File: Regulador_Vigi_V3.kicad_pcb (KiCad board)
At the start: 2 copper layers, 50 x 35 mm, 15 parts, among them J1 IN, J2 Out, U1 LM5163

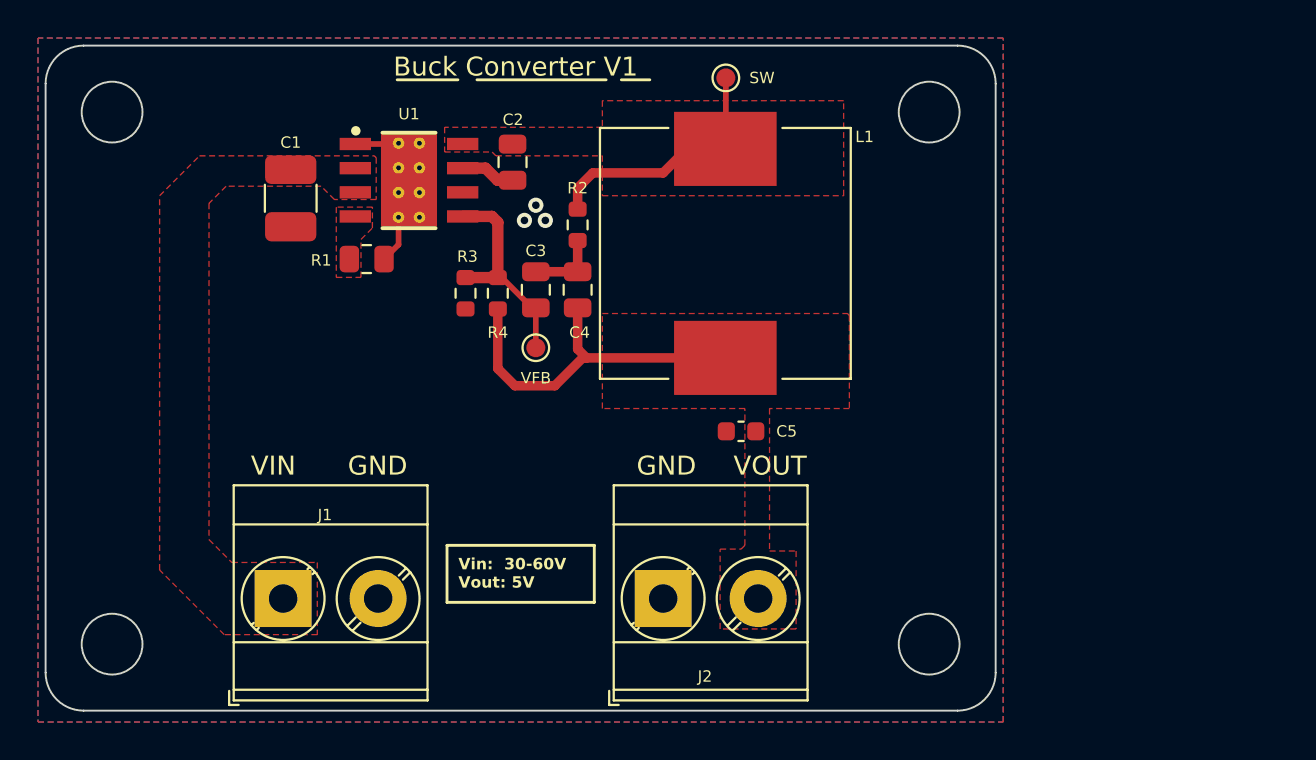
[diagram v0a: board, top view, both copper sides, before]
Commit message: SCH: Se cambiaron las resistencias del feedback, se limpiaron los comentarios. PCB: Se terminó de rutear. GITIGNORE: se agregó una línea
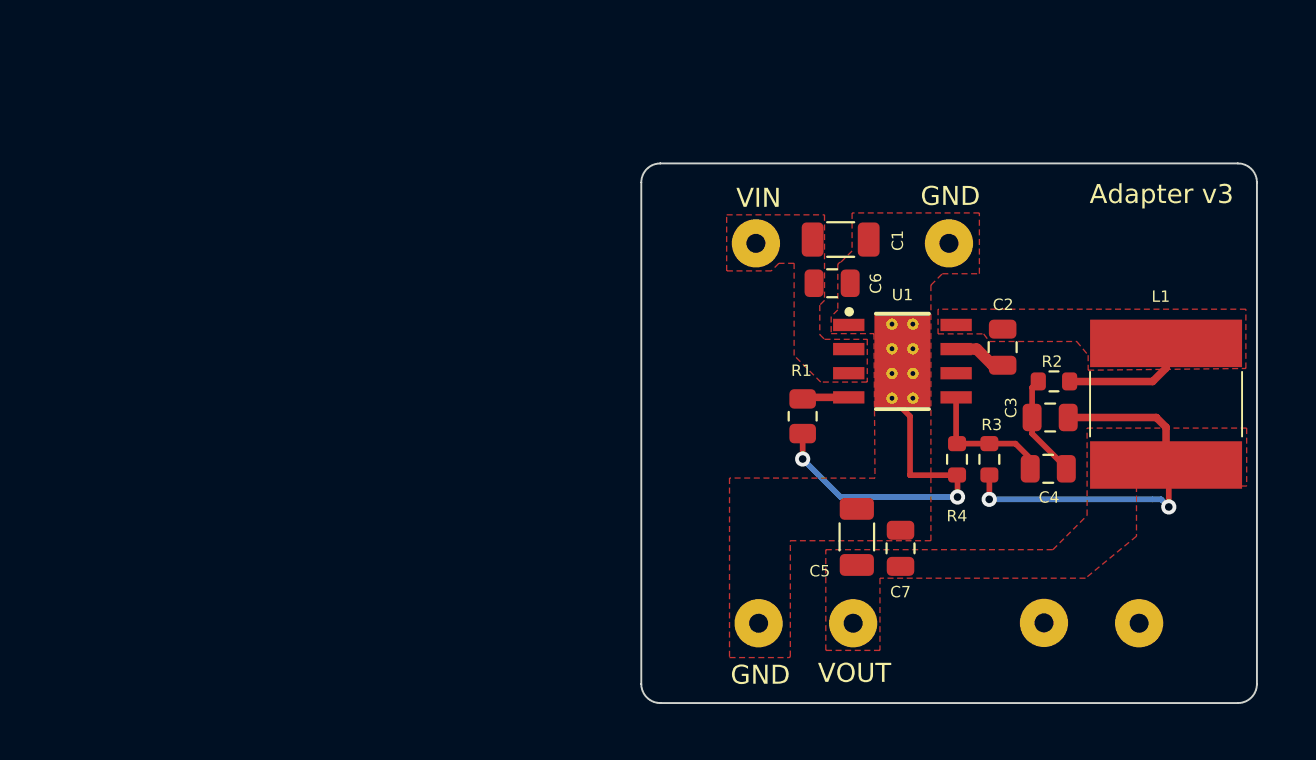
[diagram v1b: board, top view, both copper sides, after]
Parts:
- removed J1: IN, 1-Terminal-Block:AK700-DG129-1x02_P5.00mm
- removed J2: Out, 1-Terminal-Block:AK700-DG129-1x02_P5.00mm
- removed TP1: VFB, TestPoint:TestPoint_Pad_D1.0mm
- removed TP2: SW, TestPoint:TestPoint_Pad_D1.0mm
- added C6: 100nF 50V, 1-Capacitor:C_0805_2012Metric, F.Cu at (174.5, 120.5)
- added C7: 100nF 50V, 1-Capacitor:C_0805_2012Metric, F.Cu at (178.1, 134.5)
- added PAD1: PAD_2.54_1.0, 1-Pad:PAD_2.54_1.0, F.Cu at (172.7, 118.3)
- added PAD2: PAD_2.54_1.0, 1-Pad:PAD_2.54_1.0, F.Cu at (170.6, 138.4)
- added PAD3: PAD_2.54_1.0, 1-Pad:PAD_2.54_1.0, F.Cu at (175.6, 138.4)
- added PAD4: PAD_2.54_1.0, 1-Pad:PAD_2.54_1.0, F.Cu at (180.6, 118.4)
- added PAD5: PAD_2.54_1.0, 1-Pad:PAD_2.54_1.0, F.Cu at (185.6, 138.4)
- added PAD6: PAD_2.54_1.0, 1-Pad:PAD_2.54_1.0, F.Cu at (190.7, 138.4)
- C1: value 2.2uF 100V -> 4.7uF 50V; footprint 1-Capacitor:C_1210_3225Metric_Mod -> 1-Capacitor:C_1206_3216Metric
- C3: value 2.2nF 50V -> 1.2nF 50V
- C4: value 56pF 50V -> 47pF 50V
- C5: value 2.2uF 16V -> 4.7uF 50V; footprint 1-Capacitor:C_0603_1608Metric -> 1-Capacitor:C_1206_3216Metric
- L1: value SMDRI127-331MT -> 100uH 1A; footprint 1-Inductor:DR127 -> 1-Inductor:L_8x8mm
- R1: value 43k -> 150k
- R2: value 316k -> 130k
- R3: value 316k -> 210k
- R4: value 100k -> 15k
- moved C1 29.0 mm to (174.9, 118.2), turned to 0 degrees
- moved C4 28.6 mm to (185.9, 130.3), turned to 180 degrees
- moved U1 27.7 mm to (178.2, 124.6)
- moved C2 27.6 mm to (183.5, 123.9)
- moved R4 27.3 mm to (181.1, 129.8)
- moved R3 27.3 mm to (182.8, 129.8)
- moved R2 26.4 mm to (186.2, 125.7), turned to 180 degrees
- moved C3 25.8 mm to (186.0, 127.6), turned to 180 degrees
- moved L1 24.5 mm to (192.1, 126.9)
- moved R1 24.4 mm to (172.9, 127.5), turned to -90 degrees
- moved C5 8.25 mm to (175.8, 133.9), turned to 90 degrees
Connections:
- net +5V renamed VOUT
- U1 pad 10: GND -> (no net)
- U1 pad 11: GND -> (no net)
- U1 pad 12: GND -> (no net)
- U1 pad 13: GND -> (no net)
- U1 pad 14: GND -> (no net)
- U1 pad 15: GND -> (no net)
- U1 pad 16: GND -> (no net)
- U1 pad 17: GND -> (no net)
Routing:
- net GND: track 4.81 -> 18.4 mm, vias 3 -> 2
- net Net-(U1-SW): track 15.3 -> 6.67 mm
- net Net-(U1-FB): track 11.3 -> 7.18 mm
- net Net-(U1-RON): track 0.00 -> 2.46 mm
- net VOUT: track 18.9 -> 21.0 mm, vias 0 -> 2
- net Net-(C3-Pad2): track 3.84 -> 5.48 mm
- removed copper zone on B.Cu, net GND
- removed copper zone on F.Cu, net Net-(U1-RON)
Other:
- board size 50 x 35 mm -> 32.4 x 28.4 mm
- board text added: "Adapter v3"
- board text removed: "Buck Converter V1"
- board text removed: "Vin: 30-60V Vout: 5V"

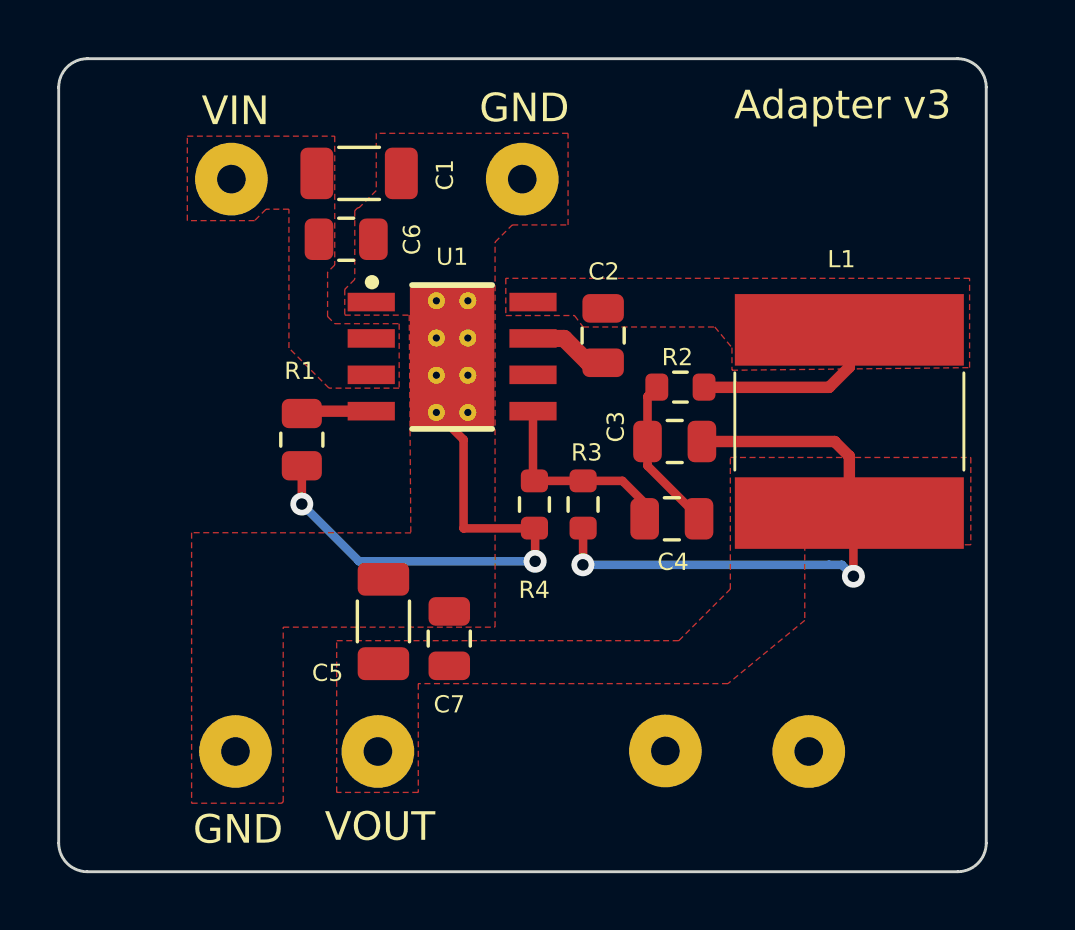
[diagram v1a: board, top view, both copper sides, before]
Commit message: SCH:Se cambió comentarios de dos capacitores iniciales para soportar mayor voltaje. PCB:Se actualiza la PCB. JLCPCB:Se cambia el código del part de los capacitores
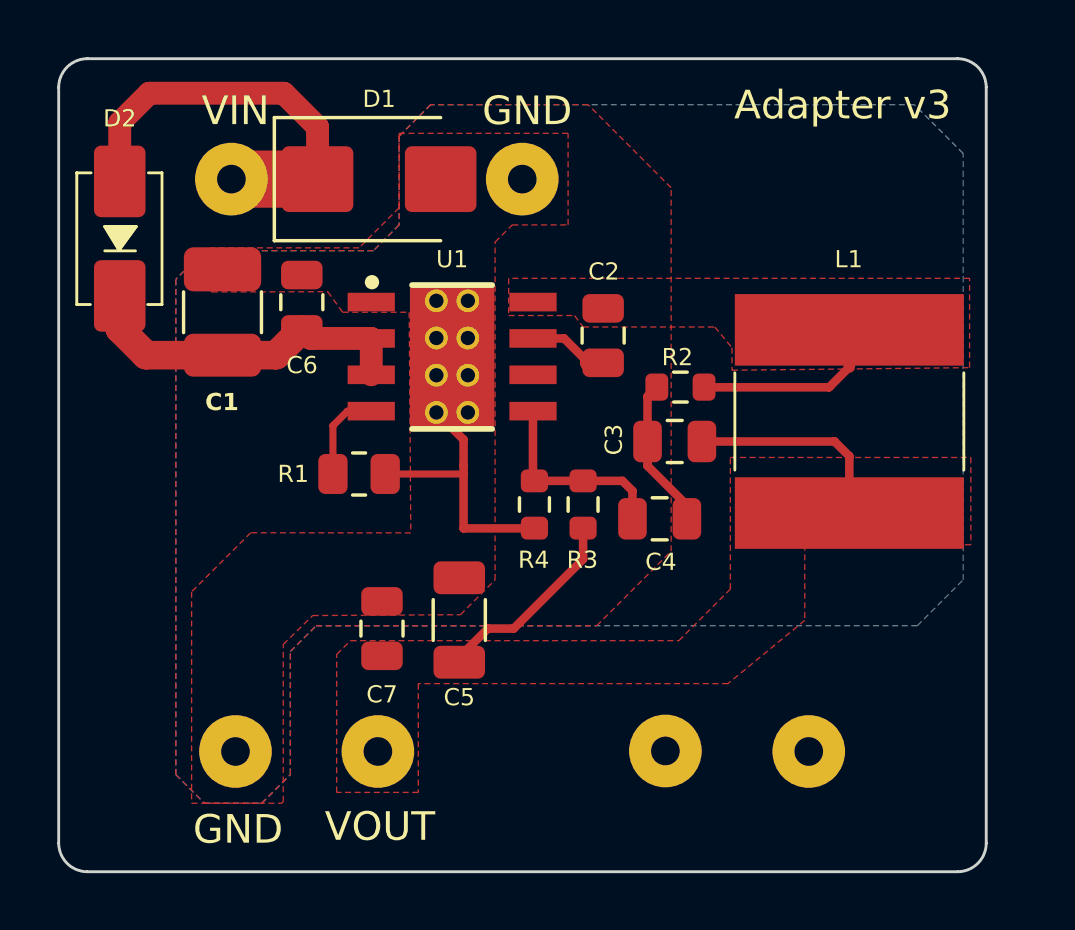
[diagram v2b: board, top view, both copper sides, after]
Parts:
- added D1: SMB39CA, Diode_SMD:D_SMB, F.Cu at (175.6, 118.4)
- added D2: M7, 1-Diode:D_SMA, F.Cu at (166.6, 120.5)
- C1: value 4.7uF 50V -> 4.7uF 100V; footprint 1-Capacitor:C_1206_3216Metric -> 1-Capacitor:C_1210_3225Metric_Mod
- C6: value 100nF 50V -> 100nF 100V
- moved C1 6.80 mm to (170.2, 123.1), turned to 90 degrees
- moved C6 2.69 mm to (172.9, 122.7), turned to 90 degrees
- moved C5 2.65 mm to (178.4, 133.8)
- moved C7 2.38 mm to (175.7, 134.1)
- moved R1 2.33 mm to (174.9, 128.7), turned to 0 degrees
- moved C4 0.42 mm to (185.4, 130.3)
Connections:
- PAD1 pad 1: VCC -> /+VIN
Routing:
- net /+VIN: track 0.00 -> 14.7 mm
- net VCC: track 0.00 -> 12.1 mm
- net GND: track 18.4 -> 9.71 mm, vias 2 -> 0
- net VOUT: track 21.0 -> 14.6 mm, vias 2 -> 0
- net Net-(U1-RON): track 2.46 -> 3.24 mm
- added copper zone on B.Cu, net GND
- removed copper zone on F.Cu, net VCC
